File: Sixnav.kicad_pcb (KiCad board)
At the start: 2 copper layers, 66 x 114.3 mm, 35 parts, among them Q1 PT908-7C-F, Q2 PT908-7C-F, Q3 PT908-7C-F, Q4 PT908-7C-F, Q5 PT908-7C-F, Q6 PT908-7C-F, U1 Pico, U2 CD4051B

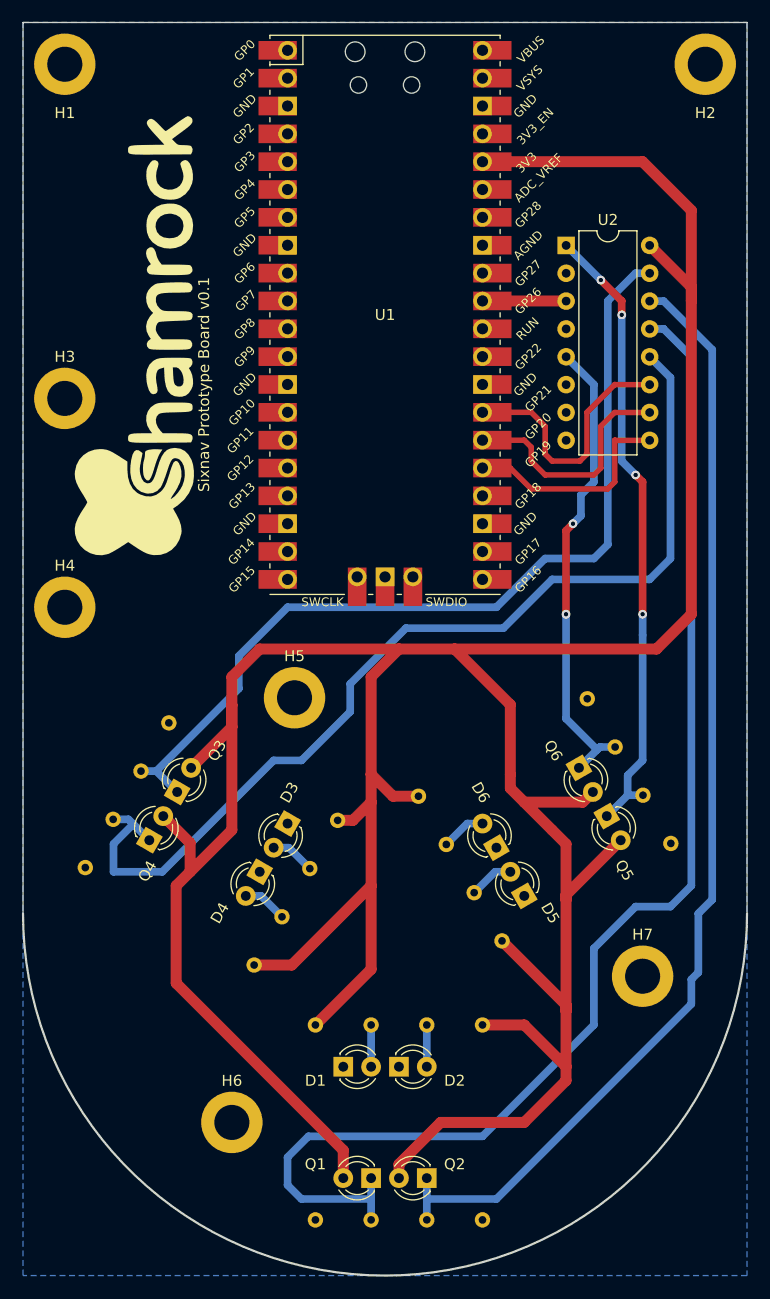
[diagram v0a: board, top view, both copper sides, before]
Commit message: Second Draft
It was only until after I finished routing this that I realized that the
PT908 and IR908 have flipped pin numbers. I'm going to have to aquire a
separate foorprint for the PT908.
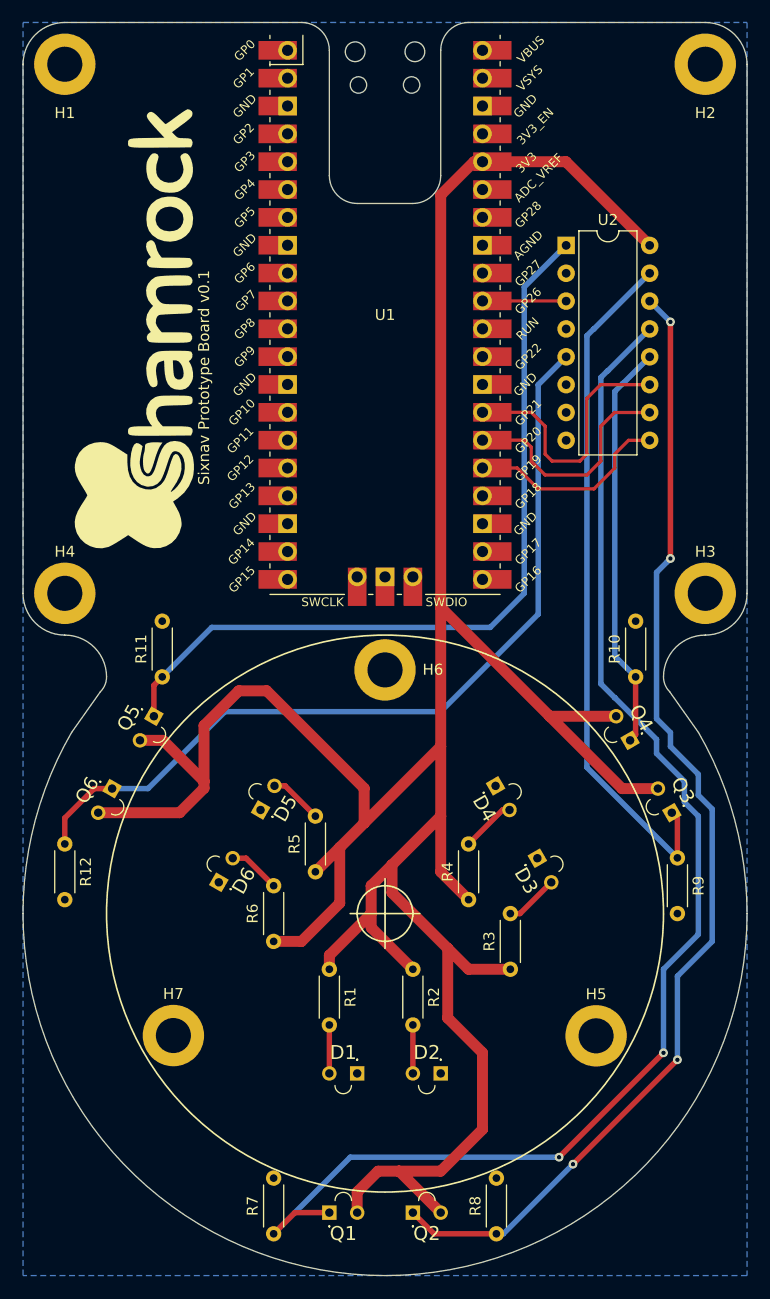
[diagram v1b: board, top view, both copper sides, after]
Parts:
- D1, D2, D3, D4, D5, D6: footprint LED_THT:LED_D3.0mm_IRGrey -> SamacSys_Parts:IR9087CF
- Q1, Q2, Q3, Q4, Q5, Q6: footprint LED_THT:LED_D3.0mm_IRBlack -> SamacSys_Parts:IR9087CF
- R1, R10, R11, R12, R2, R3, R4, R5, R6, R7, R8, R9: moved to F.Cu
- moved H3 61.1 mm to (168.9, 97.8)
- moved R12 51.0 mm to (110.5, 120.7), turned to -90 degrees
- moved R9 49.6 mm to (166.4, 121.9), turned to -90 degrees
- moved R10 49.4 mm to (162.6, 105.4), turned to 90 degrees
- moved Q3 45.2 mm to (165.9, 117.8), turned to -60 degrees
- moved R11 45.2 mm to (119.4, 105.4), turned to 90 degrees
- moved Q4 44.8 mm to (162.1, 111.2), turned to -60 degrees
- moved H6 43.6 mm to (139.7, 104.8)
- moved H7 43.1 mm to (120.4, 138.1)
- moved Q6 42.6 mm to (114.8, 115.6), turned to 60 degrees
- moved Q5 42.3 mm to (118.6, 109.0), turned to 60 degrees
- moved H5 41.3 mm to (159.0, 138.2)
- moved D6 25.5 mm to (124.5, 124.1), turned to -120 degrees
- moved D5 25.3 mm to (128.3, 117.6), turned to -120 degrees
- moved D3 23.0 mm to (153.6, 122.0), turned to 120 degrees
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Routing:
- net /MUX_X3_Q4: track 92.5 -> 37.1 mm
- net +3.3V: track 331.6 -> 276.7 mm
- net /MUX_X5_Q6: track 43.2 -> 77.8 mm, vias 2 -> 0
- net /MUX_X2_Q3: track 82.7 -> 63.5 mm
- net /MUX_X4_Q5: track 57.7 -> 73.4 mm, vias 4 -> 0
- net /MUX_X0_Q1: track 118.8 -> 121.2 mm, vias 0 -> 2
- net /MUX_X1_Q2: track 103.3 -> 105.4 mm, vias 0 -> 4
- net /MUX_C: track 20.1 -> 18.6 mm
- net /D4_A: track 4.09 -> 5.02 mm
- net /D3_A: track 4.09 -> 4.91 mm
- net /D5_A: track 4.09 -> 4.88 mm
- net /MUX_A: track 23.7 -> 24.4 mm
- net /D6_A: track 4.09 -> 4.77 mm
- net /D2_A: track 3.81 -> 4.42 mm
- net /D1_A: track 3.81 -> 4.42 mm
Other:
- outline, holes or cut-outs redrawn
- board text removed: "GP20"

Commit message: PT908 footprint
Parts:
- Q1, Q2, Q3, Q4, Q5, Q6: footprint SamacSys_Parts:IR9087CF -> SamacSys_Parts:ELPT9087C
- moved R5 11.5 mm to (134.6, 111.8), turned to -90 degrees
- moved R8 7.73 mm to (142.2, 157.5), turned to 180 degrees
- moved R6 7.73 mm to (130.8, 121.9), turned to -90 degrees
- moved R1 7.41 mm to (128.3, 135.9), turned to 0 degrees
- moved R2 6.35 mm to (137.2, 135.9), turned to 0 degrees
- moved R4 5.39 mm to (143.5, 121.9), turned to 0 degrees
- moved R3 4.58 mm to (147.3, 129.5), turned to 0 degrees
- moved R7 2.84 mm to (130.8, 153.7), turned to 180 degrees
- moved R10 1.27 mm to (162.6, 106.7)
- moved R11 1.27 mm to (120.7, 105.4)
- moved D4 0.82 mm to (149.0, 115.0)
- moved Q4 0.82 mm to (161.3, 110.8), turned to 120 degrees
- moved D6 0.82 mm to (124.7, 125.0)
- moved Q6 0.82 mm to (114.9, 116.4), turned to -120 degrees
- moved D5 0.81 mm to (129.1, 117.3)
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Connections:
- U1 pad 13: unconnected-(U1-Pad13) -> GND
- U1 pad 18: unconnected-(U1-Pad18) -> GND
- U1 pad 3: unconnected-(U1-Pad3) -> GND
- U1 pad 33: unconnected-(U1-Pad33) -> GND
- U1 pad 8: unconnected-(U1-Pad8) -> GND
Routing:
- net +3.3V: track 276.7 -> 285.4 mm
- net /MUX_X5_Q6: track 77.8 -> 85.0 mm
- net /MUX_X1_Q2: track 105.4 -> 109.3 mm
- net /MUX_X2_Q3: track 63.5 -> 59.8 mm
- net /MUX_X0_Q1: track 121.2 -> 117.6 mm
- net /D6_A: track 4.77 -> 6.63 mm
- net /MUX_A: track 24.4 -> 22.9 mm
- net /MUX_X4_Q5: track 73.4 -> 72.1 mm
- net /D1_A: track 4.42 -> 5.46 mm
- net /D2_A: track 4.42 -> 5.46 mm
- net /MUX_B: track 21.5 -> 20.8 mm
- net /D3_A: track 4.91 -> 5.64 mm

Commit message: First JLCPCB order
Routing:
- net /MUX_X0_Q1: vias 2 -> 0
- net /MUX_X1_Q2: vias 4 -> 2
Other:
- board text added: "JLCJLCJLCJLC"
